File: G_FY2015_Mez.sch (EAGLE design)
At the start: 244 parts, among them IC100 FT232RL, IC101 FT245RL, J100 EPL.00.250.NTN, J101 IL-2P-S3EN2, J110 EPL.00.250.NTN, J111 IL-2P-S3EN2, J120 EPL.00.250.NTN, J121 IL-2P-S3EN2, J130 EPL.00.250.NTN, J131 IL-2P-S3EN2, J180 TOKUDEN_SP6, J181 USB Mini-B Connector, J182 USB Mini-B Connector, J300 SHV_PIGTAIL_LAND, J301 SHV_PIGTAIL_LAND, J400 RPI2_GPIO_HOLES, J410 IL-3P-S3EN2, J411 IL-3P-S3EN2, J600_12V IL-4P-S3EN2, J610 2.1MMJACKTHM, J620 IL-2P-S3EN2, J630 USB_TYPEA_LUMBERG_2410_01, J640 USB_TYPEA_LUMBERG_2410_01, J650_VOUT IL-4P-S3EN2, U100 AD9215LONG_PAD, U101 AD8138, U102 LM6172, U110 AD9215LONG_PAD, U111 AD8138, U112 LM6172, U120 AD9215LONG_PAD, U121 AD8138, U130 AD9215LONG_PAD, U131 AD8138, U191 GPS_FGPMMOPA6H, U300 OPTON_1PA_12, U301 OPTON_1PA_12, U302 2SC1815, U303 2SJ681, U410 MCP3208-CI/SL, U411 MCP1525TSOT-23-3, U412 LM60, U413 LM60, U500 LT6106, U510 LT6106, U520 2SC1815, U521 2SJ681, U600 PHT12050WAH, U610 PHT12050WAH, U620 LTC1983ES6-3, U621 LTC1983ES6-5

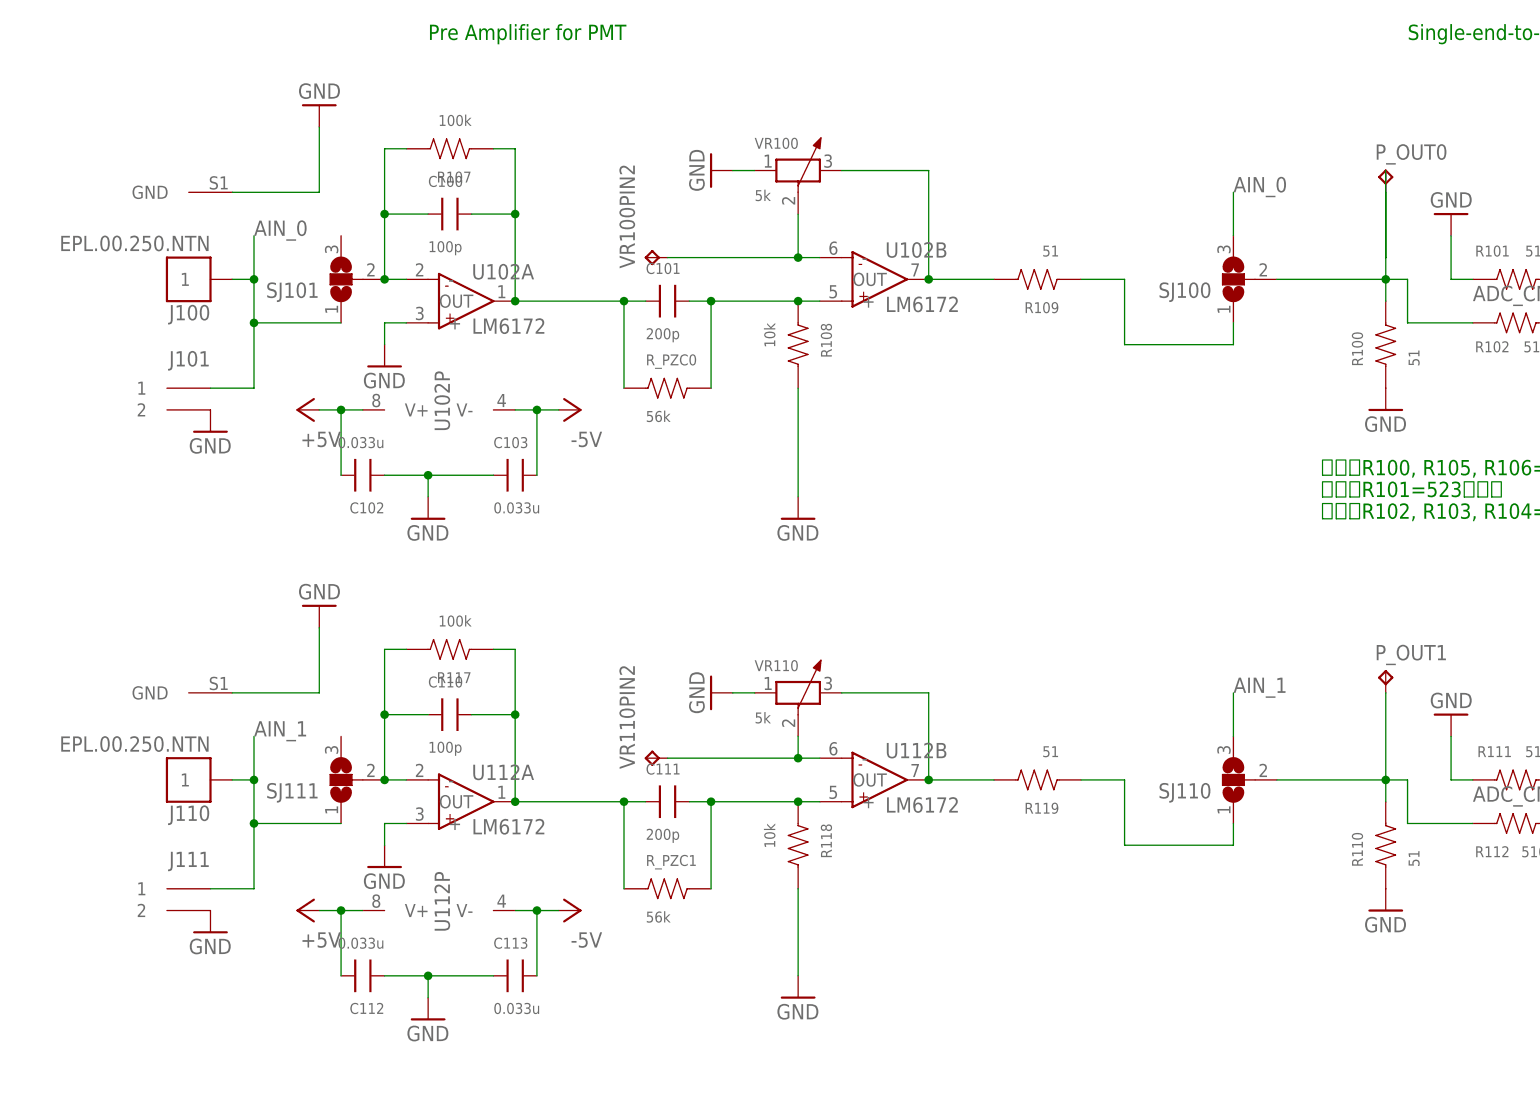
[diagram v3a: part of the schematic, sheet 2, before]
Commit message: Ch.0 and Ch.1 connector modified, slow ADC and Ras Pi locations modified
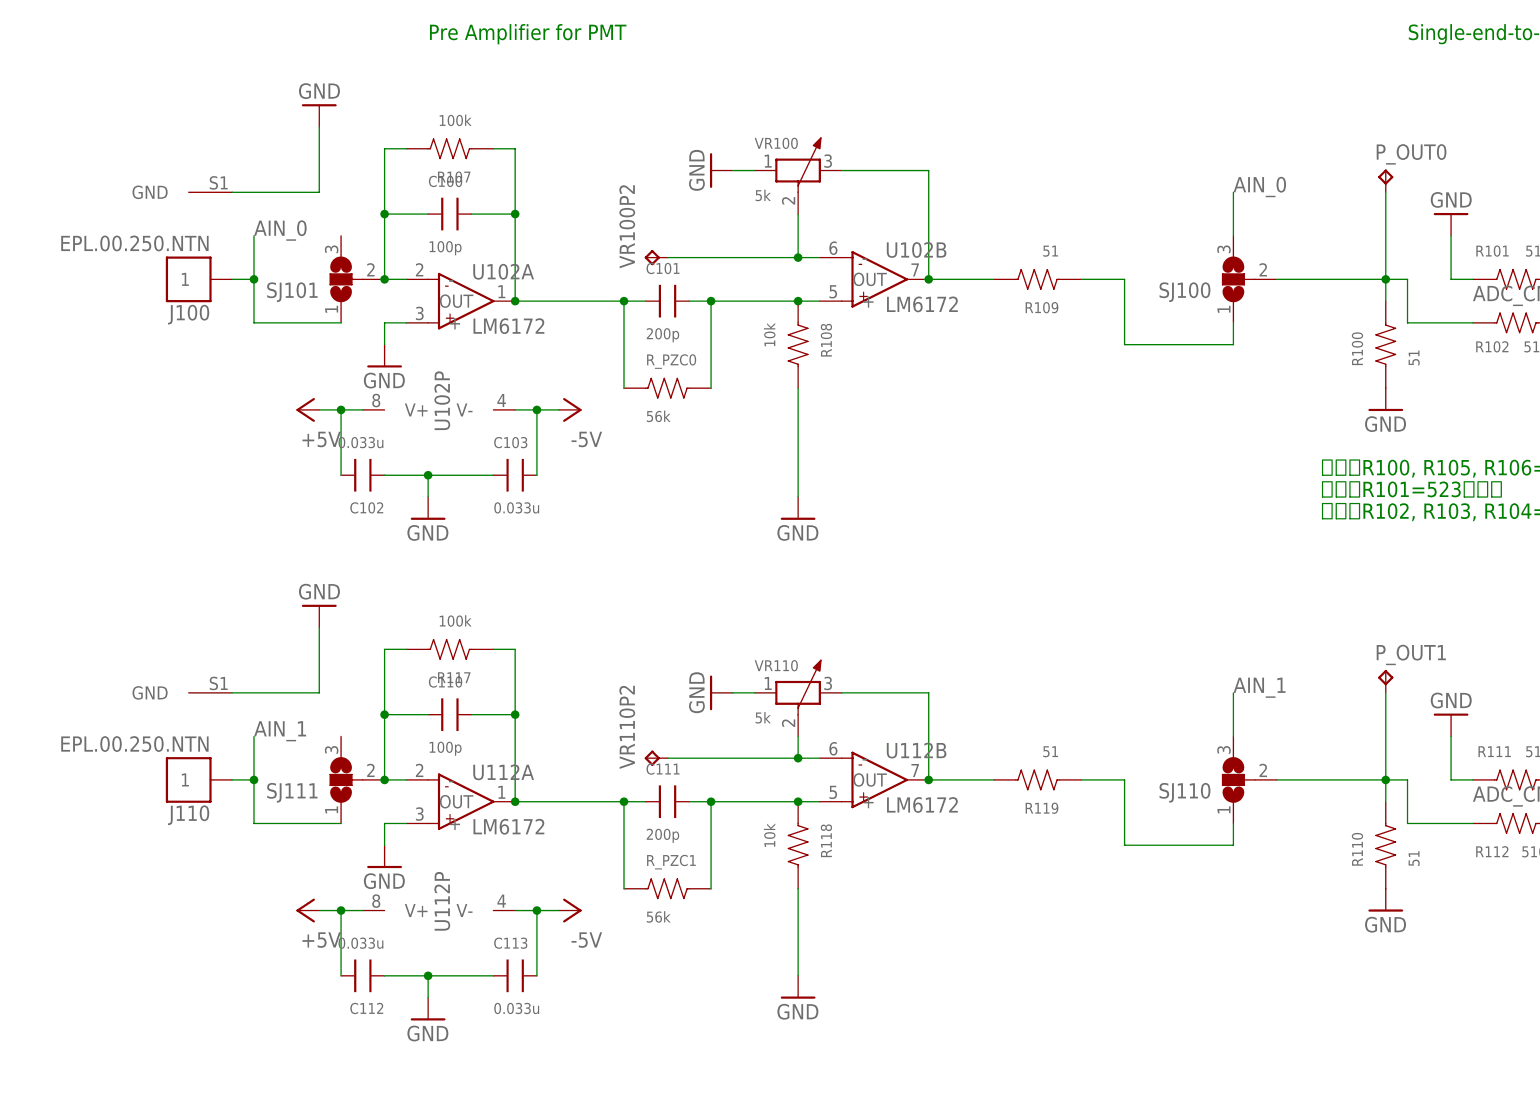
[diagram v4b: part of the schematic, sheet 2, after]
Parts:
- removed J101, J111: IL-2P-S3EN2, Aardvark:IL-2P-S3EN2
- renumbered VR100PIN2 to VR100P2, VR110PIN2 to VR110P2
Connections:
- net AIN_0: no longer J101.1
- net AIN_1: no longer J111.1
- net GND: no longer J101.2, J111.2
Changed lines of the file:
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@@
 <part name="+3V16" library="Aardvark" deviceset="+3V3" device=""/>
 <part name="SJ100" library="Aardvark" deviceset="SJ2W" device="W"/>
-<part name="J111" library="Aardvark" deviceset="IL-2P-S3EN2" device=""/>
 <part name="J121" library="Aardvark" deviceset="IL-2P-S3EN2" device=""/>
 <part name="J131" library="Aardvark" deviceset="IL-2P-S3EN2" device=""/>
-<part name="J101" library="Aardvark" deviceset="IL-2P-S3EN2" device=""/>
-<part name="GND93" library="Aardvark" deviceset="GND" device=""/>
 <part name="GND94" library="Aardvark" deviceset="GND" device=""/>
 <part name="GND95" library="Aardvark" deviceset="GND" device=""/>
-<part name="GND96" library="Aardvark" deviceset="GND" device=""/>
 <part name="VR100" library="Aardvark" deviceset="DIP-TRIMMER-10K-10%-1/2W(3P-9.7X5.0X9.80MM)" device="" value="5k"/>
 <part name="VR110" library="Aardvark" deviceset="DIP-TRIMMER-10K-10%-1/2W(3P-9.7X5.0X9.80MM)" device="" value="5k"/>
@@
 <part name="R400" library="Aardvark" deviceset="R2012" device="" value="680"/>
 <part name="GND45" library="Aardvark" deviceset="GND" device=""/>
-<part name="VR100PIN2" library="Aardvark" deviceset="TP" device="PAD1-13"/>
-<part name="VR110PIN2" library="Aardvark" deviceset="TP" device="PAD1-13"/>
+<part name="VR100P2" library="Aardvark" deviceset="TP" device="PAD1-13"/>
+<part name="VR110P2" library="Aardvark" deviceset="TP" device="PAD1-13"/>
 <part name="VR_HV0" library="Aardvark" deviceset="TP" device="PAD1-13"/>
 <part name="VR_HV1" library="Aardvark" deviceset="TP" device="PAD1-13"/>
@@
 <instance part="U$36" gate="G$1" x="129.54" y="-48.26" rot="R270"/>
 <instance part="SJ100" gate="G$1" x="-160.02" y="111.76" rot="R180"/>
-<instance part="J111" gate="G$1" x="-281.94" y="38.1" rot="MR0"/>
 <instance part="J121" gate="G$1" x="-281.94" y="-27.94" rot="MR0"/>
 <instance part="J131" gate="G$1" x="-281.94" y="-86.36" rot="MR0"/>
-<instance part="J101" gate="G$1" x="-281.94" y="96.52" rot="MR0"/>
-<instance part="GND93" gate="1" x="-279.4" y="35.56"/>
 <instance part="GND94" gate="1" x="-279.4" y="-30.48"/>
 <instance part="GND95" gate="1" x="-279.4" y="-88.9"/>
-<instance part="GND96" gate="1" x="-279.4" y="93.98"/>
 <instance part="VR100" gate="G$1" x="-210.82" y="124.46"/>
 <instance part="VR110" gate="G$1" x="-210.82" y="63.5"/>
@@
 <instance part="R_PZC1" gate="R" x="-226.06" y="40.64"/>
 <instance part="U$42" gate="G$1" x="99.06" y="-127" rot="R90"/>
-<instance part="VR100PIN2" gate="G$1" x="-228.6" y="114.3" rot="R90"/>
-<instance part="VR110PIN2" gate="G$1" x="-228.6" y="55.88" rot="R90"/>
+<instance part="VR100P2" gate="G$1" x="-228.6" y="114.3" rot="R90"/>
+<instance part="VR110P2" gate="G$1" x="-228.6" y="55.88" rot="R90"/>
 </instances>
 <busses>
@@
 </segment>
 <segment>
-<pinref part="GND96" gate="1" pin="GND"/>
-<pinref part="J101" gate="G$1" pin="2"/>
-</segment>
-<segment>
-<pinref part="GND93" gate="1" pin="GND"/>
-<pinref part="J111" gate="G$1" pin="2"/>
-</segment>
-<segment>
 <pinref part="GND94" gate="1" pin="GND"/>
 <pinref part="J121" gate="G$1" pin="2"/>
@@
 <pinref part="J100" gate="G$1" pin="1"/>
 <wire x1="-274.32" y1="111.76" x2="-276.86" y2="111.76" width="0.1524" layer="91"/>
-<wire x1="-279.4" y1="99.06" x2="-274.32" y2="99.06" width="0.1524" layer="91"/>
-<wire x1="-274.32" y1="99.06" x2="-274.32" y2="106.68" width="0.1524" layer="91"/>
 <junction x="-274.32" y="111.76"/>
-<pinref part="J101" gate="G$1" pin="1"/>
 <wire x1="-274.32" y1="106.68" x2="-274.32" y2="111.76" width="0.1524" layer="91"/>
 <wire x1="-274.32" y1="111.76" x2="-274.32" y2="116.84" width="0.1524" layer="91"/>
@@
 <pinref part="SJ101" gate="G$1" pin="1"/>
 <wire x1="-264.16" y1="106.68" x2="-274.32" y2="106.68" width="0.1524" layer="91"/>
-<junction x="-274.32" y="106.68"/>
 </segment>
 <segment>
@@
 <wire x1="-139.7" y1="106.68" x2="-132.08" y2="106.68" width="0.1524" layer="91"/>
 <pinref part="P_OUT0" gate="G$1" pin="TP"/>
-<wire x1="-142.24" y1="111.76" x2="-142.24" y2="114.3" width="0.1524" layer="91"/>
-<wire x1="-142.24" y1="114.3" x2="-142.24" y2="121.92" width="0.1524" layer="91"/>
-<wire x1="-142.24" y1="114.3" x2="-142.24" y2="124.46" width="0.1524" layer="91"/>
+<wire x1="-142.24" y1="111.76" x2="-142.24" y2="121.92" width="0.1524" layer="91"/>
 </segment>
 </net>
@@
 <junction x="-274.32" y="53.34"/>
 <wire x1="-274.32" y1="53.34" x2="-274.32" y2="58.42" width="0.1524" layer="91"/>
-<wire x1="-274.32" y1="40.64" x2="-274.32" y2="48.26" width="0.1524" layer="91"/>
 <wire x1="-274.32" y1="48.26" x2="-274.32" y2="53.34" width="0.1524" layer="91"/>
-<wire x1="-279.4" y1="40.64" x2="-274.32" y2="40.64" width="0.1524" layer="91"/>
-<pinref part="J111" gate="G$1" pin="1"/>
 <label x="-274.32" y="58.42" size="1.778" layer="95"/>
 <pinref part="SJ111" gate="G$1" pin="1"/>
 <wire x1="-264.16" y1="48.26" x2="-274.32" y2="48.26" width="0.1524" layer="91"/>
-<junction x="-274.32" y="48.26"/>
 </segment>
 </net>
@@
 <pinref part="U102" gate="B" pin="-"/>
 <wire x1="-226.06" y1="114.3" x2="-210.82" y2="114.3" width="0.1524" layer="91"/>
-<pinref part="VR100PIN2" gate="G$1" pin="TP"/>
+<pinref part="VR100P2" gate="G$1" pin="TP"/>
 <pinref part="VR100" gate="G$1" pin="2"/>
 <wire x1="-210.82" y1="114.3" x2="-208.28" y2="114.3" width="0.1524" layer="91"/>
@@
 <pinref part="U112" gate="B" pin="-"/>
 <wire x1="-210.82" y1="55.88" x2="-208.28" y2="55.88" width="0.1524" layer="91"/>
-<pinref part="VR110PIN2" gate="G$1" pin="TP"/>
+<pinref part="VR110P2" gate="G$1" pin="TP"/>
 <wire x1="-226.06" y1="55.88" x2="-210.82" y2="55.88" width="0.1524" layer="91"/>
 <junction x="-210.82" y="55.88"/>
